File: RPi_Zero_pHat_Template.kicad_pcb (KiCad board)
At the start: 2 copper layers, 65 x 30.5 mm, 6 parts, among them J1 RPi_GPIO, J2 RPi_GPIO

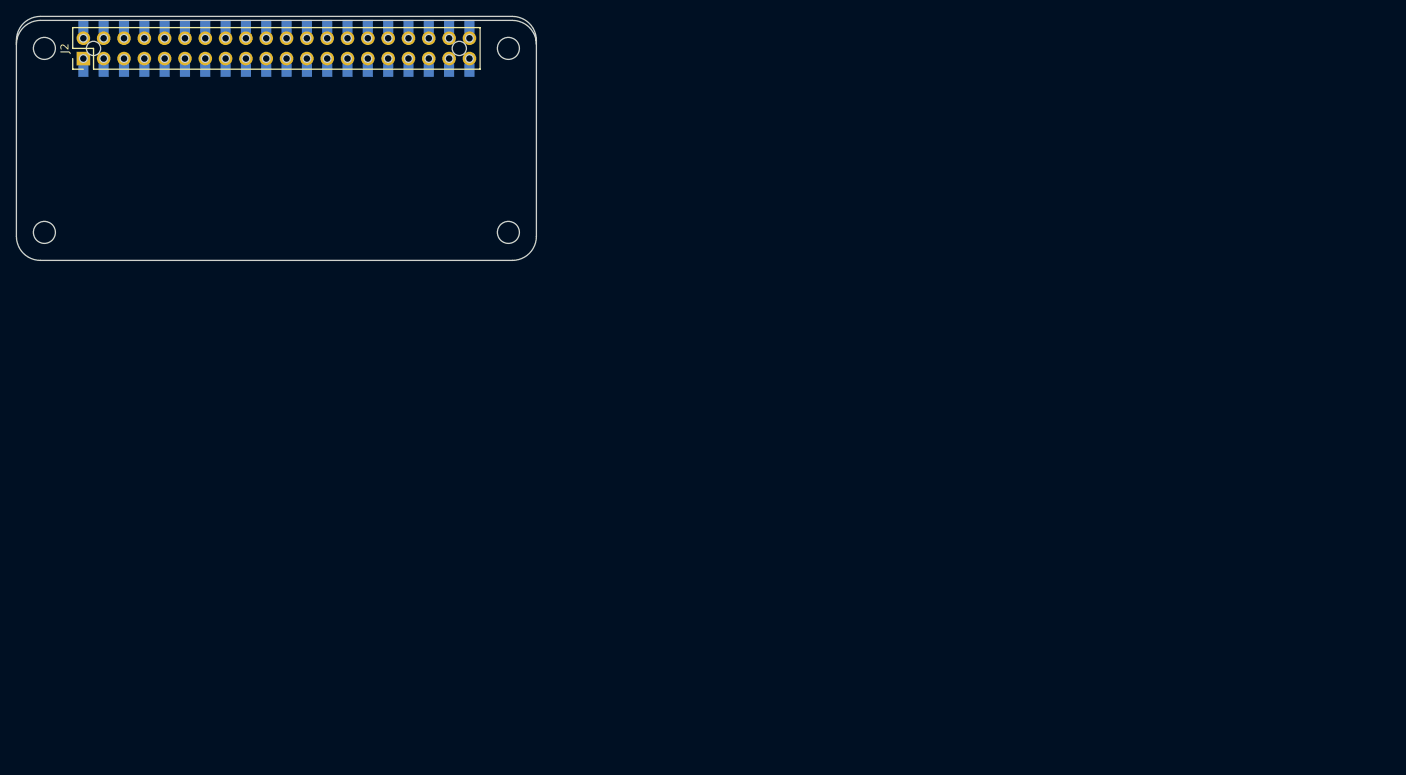
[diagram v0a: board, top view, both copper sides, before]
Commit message: PCB: Updated with new through-hole selection
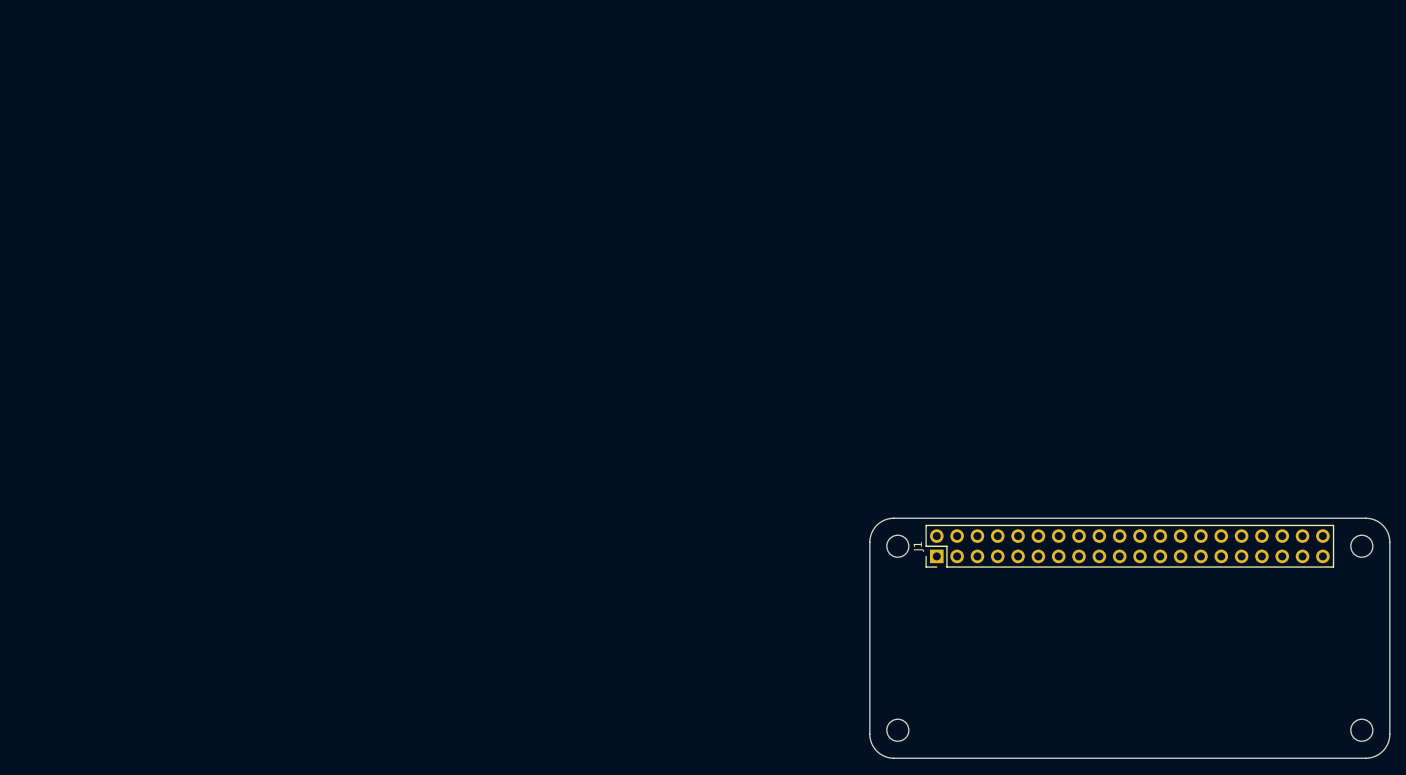
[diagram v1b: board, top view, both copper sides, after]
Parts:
- removed J2: RPi_GPIO, Connector_PinHeader_2.54mm:PinHeader_2x20_P2.54mm_Vertical
- J1: footprint Connector_Samtec_HLE_SMD-ML:Samtec_HLE-120-02-xxx-DV-BE-A_2x20_RPi_Bottom -> Connector_PinHeader_2.54mm:PinHeader_2x20_P2.54mm_Vertical; moved to F.Cu
- moved ? 123.5 mm to (122.7, 113.2)
- moved ? 123.5 mm to (180.7, 90.2)
- moved ? 123.5 mm to (180.7, 113.2)
- moved ? 123.5 mm to (122.7, 90.2)
- moved J1 104.1 mm to (127.5, 91.5), turned to 90 degrees
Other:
- board size 65 x 30.5 mm -> 65 x 30 mm
- board text removed: "Select one of these board edges depending upon the type of socket that is used."
